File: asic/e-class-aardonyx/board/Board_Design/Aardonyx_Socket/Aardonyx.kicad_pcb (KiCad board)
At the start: 4 copper layers, 188.6 x 147.6 mm, 327 parts, among them J1 USB_B_6PIN, J10 Conn_1x6, J11 Conn_1x6, J12 Conn_1x3_M, J13 Conn_1x8_F, J14 Conn_1x6_F, J15 Conn_1x10_F, J16 Conn_1x8_F, J17 USB_OTG, J18 Conn_1x3_M, J19 Conn_1x3_M, J2 Conn_1x8, J3 Conn_1x3_M, J4 Conn_1x4, J5 PJ-202H PWRJACK, J6 Conn_1x3_M, J7 Conn_1x4, J8 Conn_1x3_M, J9 Conn_1x8, Q1 FDN339AN, SW1 SW_SPST, SW2 FSM2JSMAATR, SW3 SW_DIP_x03, U1 FT2232H, U10 TPS7A7002DDAR, U11 ADM1186, U13 TPS7A7002DDAR, U14 74AUP1G09GW, U15 SKT32E, U16 93LC56BT-I_OT, U2 IS42S32160F-TSOP2, U3 CDCE913PW, U4 TPS54627DDAR, U5 CAT24M01WI-GT3, U6 IS25LP256x-xM, U7 ADC128S102CIMTX/NOPB, U8 LSF0108PWR, U9 LSF0108PWR, Y1 12MHz, Y2 27MHz

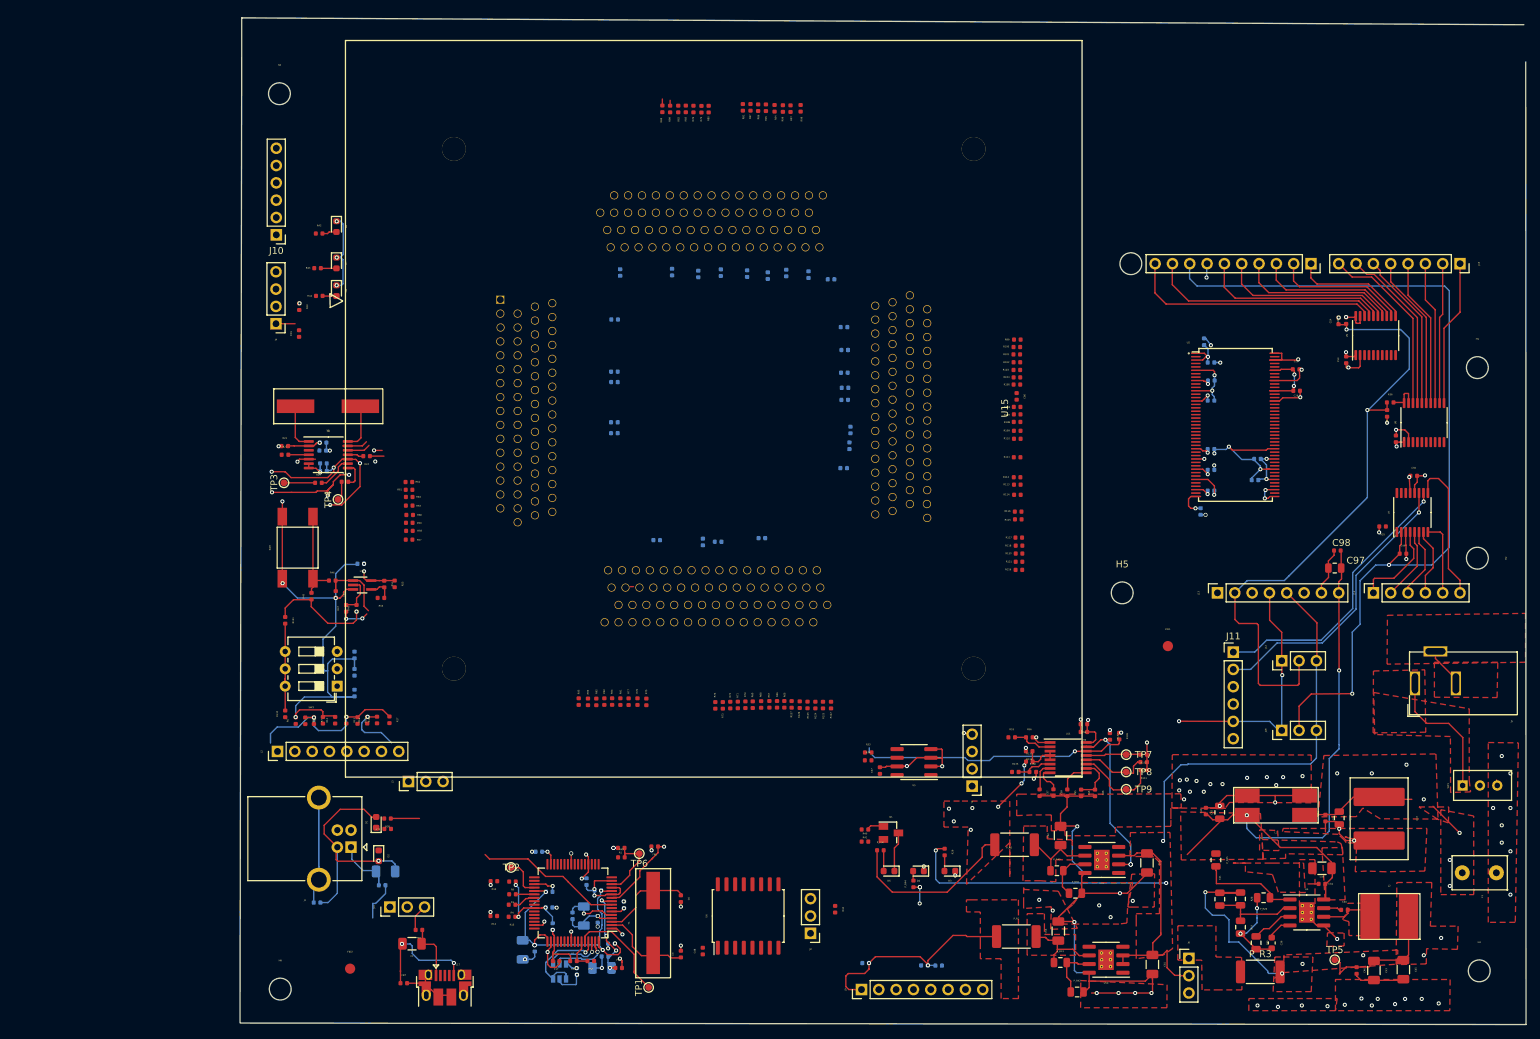
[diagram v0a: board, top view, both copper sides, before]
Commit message: updated socket com placement
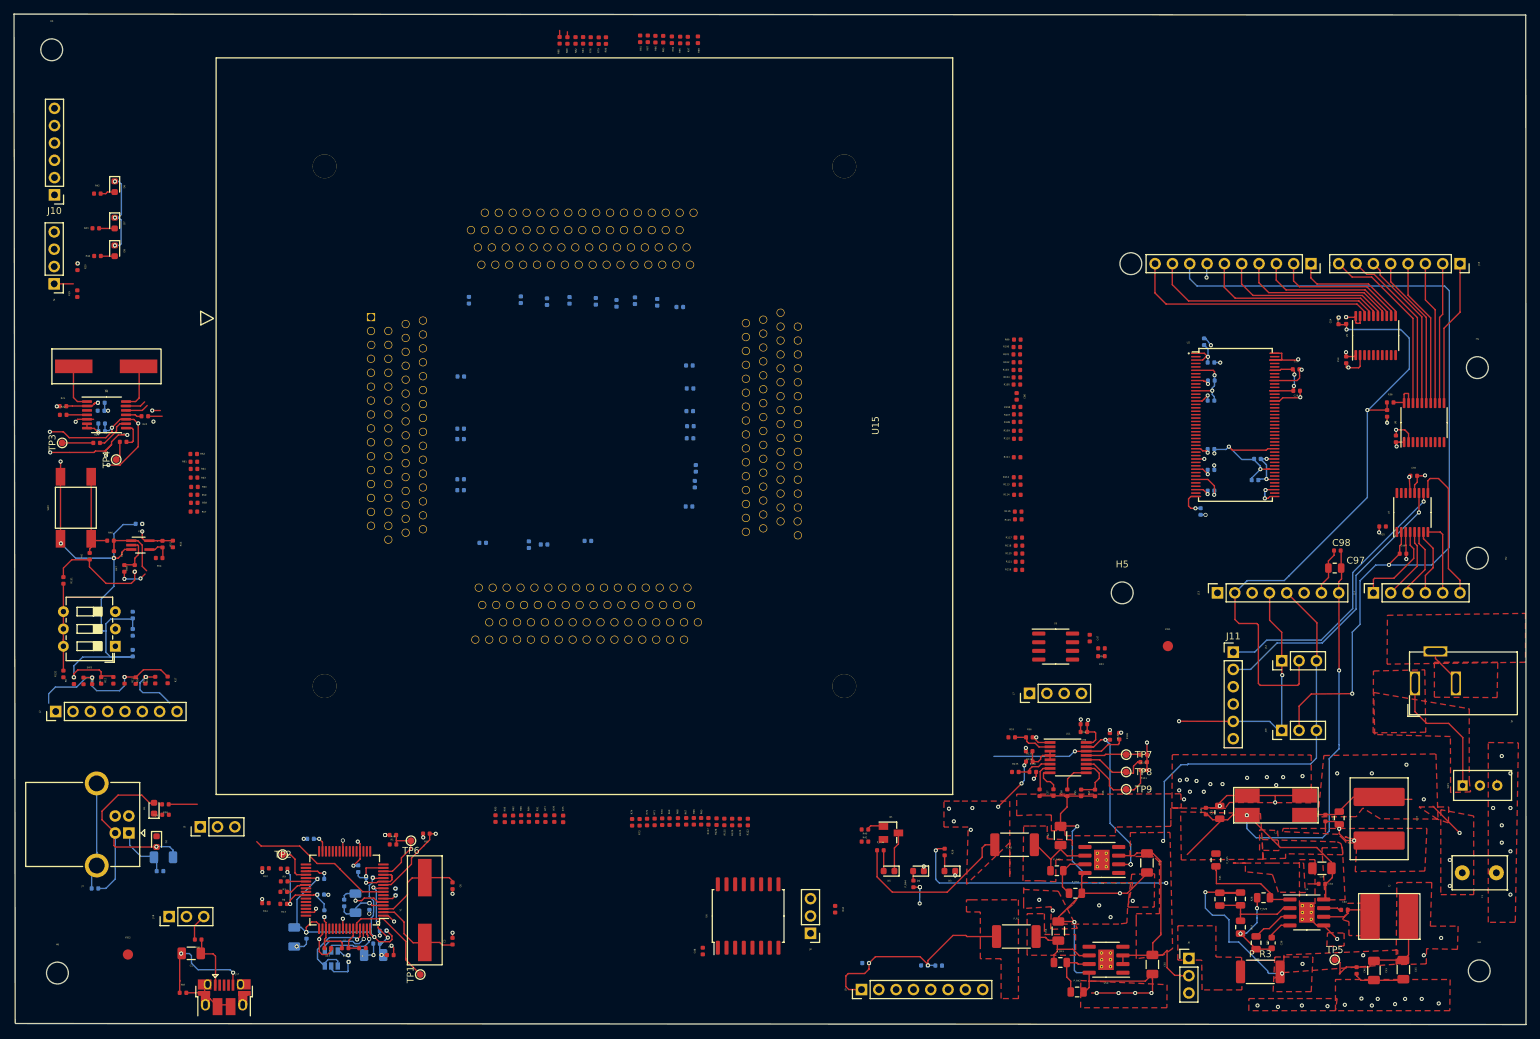
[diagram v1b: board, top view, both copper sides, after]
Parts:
- moved R34 37.9 mm to (218.2, 107.4), turned to 180 degrees
- moved R33 37.0 mm to (218.2, 108.5), turned to 180 degrees
- moved C47 36.4 mm to (216.4, 105.9), turned to 270 degrees
- moved H3 34.0 mm to (64.2, 19.6)
- moved C2 33.5 mm to (99.8, 149.7)
- moved C8 33.5 mm to (111.9, 150.7)
- moved R13 33.5 mm to (98.3, 144.9)
- moved R14 33.5 mm to (95.6, 144.8)
- moved C10 33.5 mm to (107.1, 144.7)
- moved C12 33.5 mm to (103.7, 141.2)
- moved C13 33.5 mm to (112.8, 148.8)
- moved C16 33.5 mm to (103.7, 143.5)
- moved C3 33.5 mm to (123.0, 150.3)
- moved C4 33.5 mm to (101.6, 149.5)
- moved C5 33.5 mm to (111.5, 152.4)
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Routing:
- net /power_2/RESET_ASIC: track 44.0 -> 24.4 mm
- net GND: track 506.5 -> 489.5 mm, vias 118 -> 115
- net VBUS_USB1: track 5.79 -> 0.00 mm
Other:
- board size 188.6 x 147.6 mm -> 221.7 x 148.2 mm

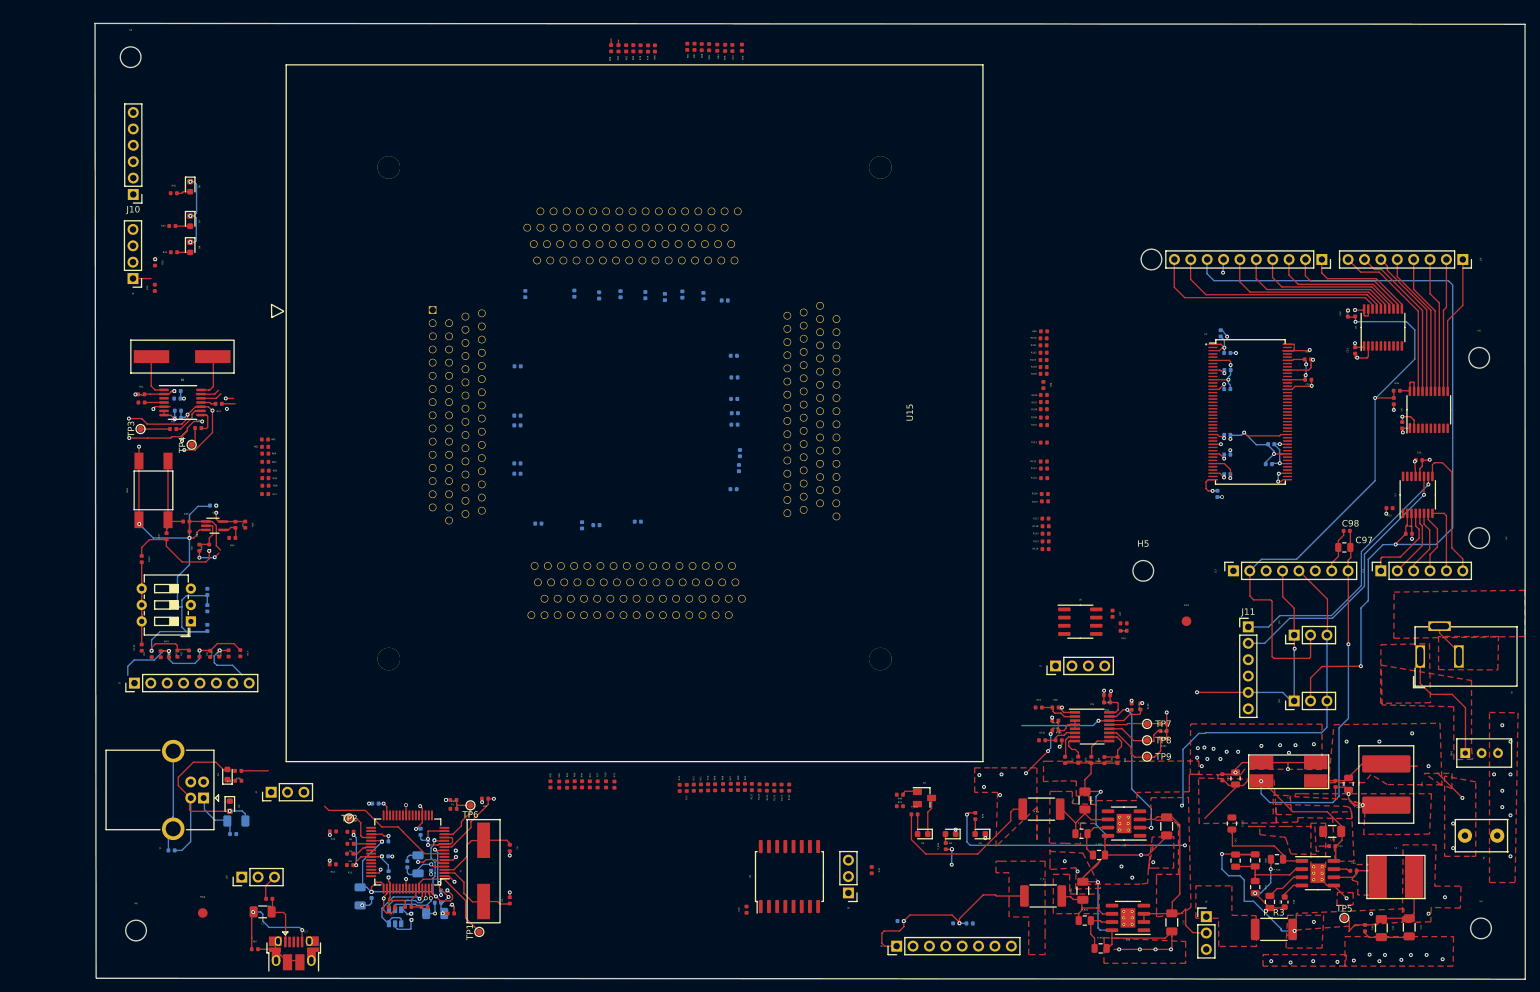
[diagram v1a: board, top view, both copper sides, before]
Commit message: update socket compo placement
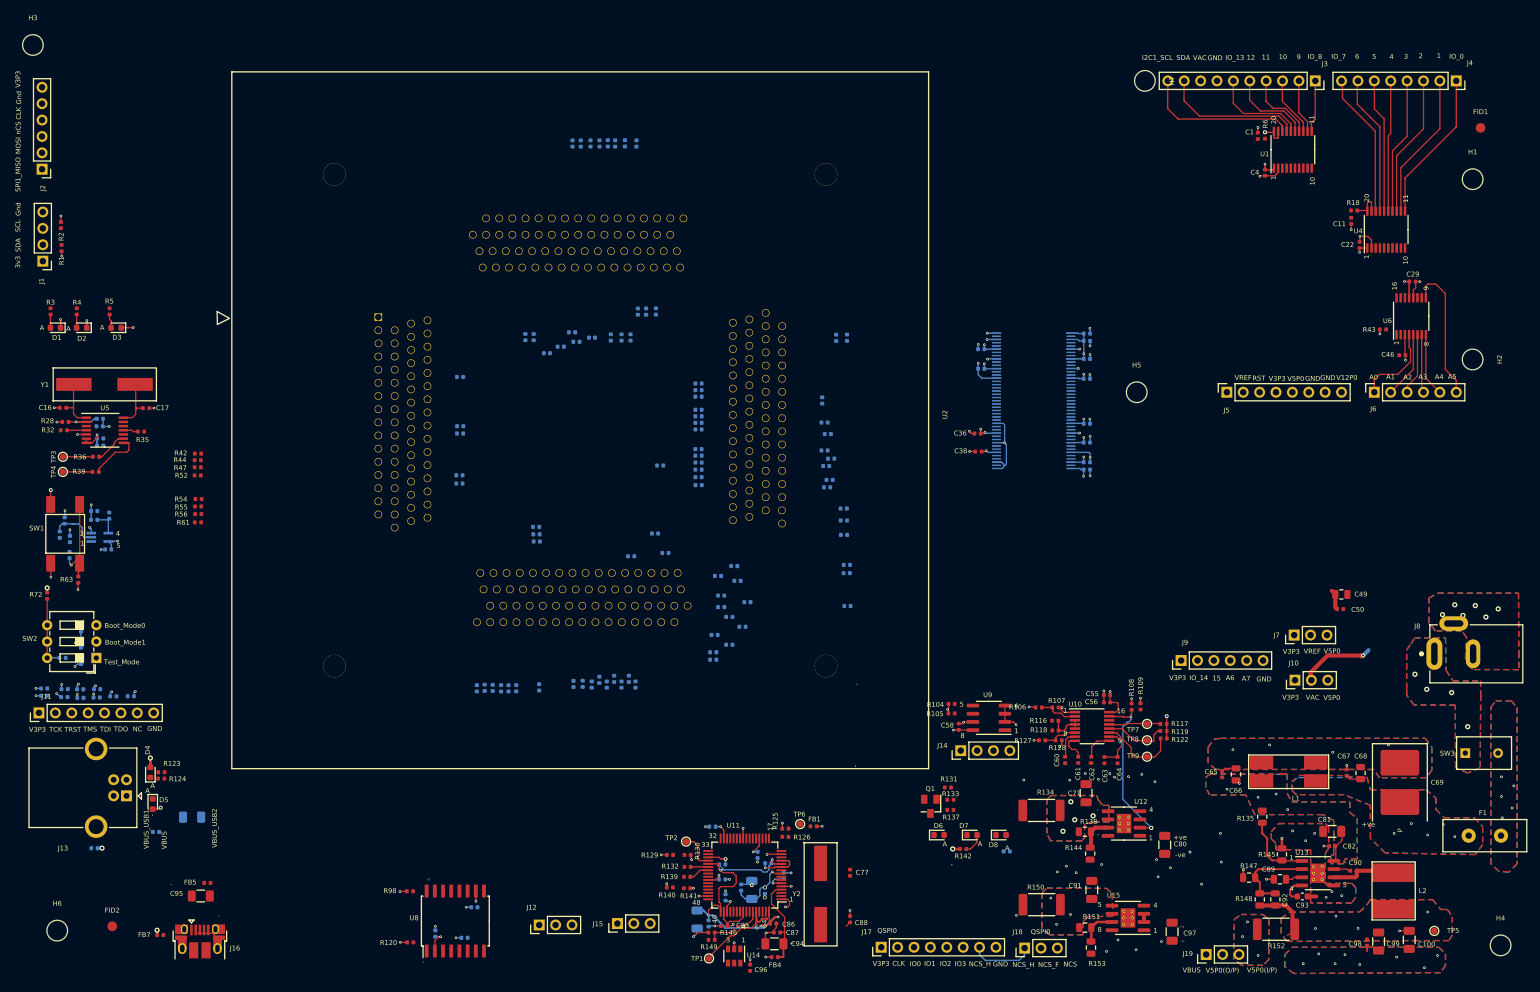
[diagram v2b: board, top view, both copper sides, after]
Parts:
- removed the C1 at (84.7, 152.1)
- removed the C10 at (107.1, 144.7)
- removed the C11 at (110.9, 141.0)
- removed the C12 at (103.7, 141.2)
- removed the C13 at (112.8, 148.8)
- removed the C15 at (102.2, 135.3)
- removed the C19 at (234.2, 65.5)
- removed the C2 at (99.8, 149.7)
- removed the C32 at (71.6, 75.6)
- removed the C36 at (243.1, 150.6)
- removed the C4 at (101.6, 149.5)
- removed the C47 at (216.4, 105.9)
- removed the C48 at (159.7, 151.8)
- removed the C5 at (111.5, 152.4)
- removed the C7 at (104.2, 146.3)
- removed the C71 at (124.2, 84.2)
- removed the C8 at (111.9, 150.7)
- removed the C9 at (108.8, 144.8)
- removed the D6 at (73.5, 39.7)
- removed the D7 at (73.5, 45.0)
- removed the D8 at (73.5, 49.1)
- removed the FB3 at (110.8, 145.2)
- removed the J10 at (64.7, 40.9)
- removed the J3 at (86.0, 133.6)
- removed the J4 at (64.6, 54.0)
- removed the J7 at (207.6, 114.0)
- removed the J8 at (175.5, 149.2)
- removed the R1 at (114.3, 134.8)
- removed the R10 at (95.6, 139.7)
- removed the R115 at (206.0, 88.5)
- removed the R116 at (205.9, 87.4)
- removed the R119 at (206.1, 95.9)
- removed the R14 at (95.6, 144.8)
- removed the R142 at (183.6, 153.5)
- removed the R20 at (68.0, 51.5)
- removed the R21 at (65.9, 71.9)
- removed the R30 at (194.3, 153.9)
- removed the R31 at (192.2, 153.9)
- removed the R32 at (179.1, 145.7)
- removed the R33 at (218.2, 108.5)
- removed the R34 at (218.2, 107.4)
- removed the R43 at (70.7, 45.8)
- removed the R44 at (71.0, 49.9)
- removed the R49 at (114.3, 136.2)
- removed the R50 at (109.8, 151.4)
- removed the R52 at (107.3, 151.4)
- removed the R62 at (85.1, 78.9)
- removed the R72 at (151.5, 132.9)
- removed the R8 at (71.5, 112.1)
- removed the R80 at (145.5, 18.3)
- removed the R83 at (142.2, 18.3)
- removed the R9 at (98.3, 139.7)
- removed the U1 at (107.2, 142.8)
- removed the U15 at (142.4, 74.8)
- removed the U5 at (211.5, 107.1)
- removed the U6 at (166.4, 146.6)
- removed the Y1 at (119.0, 145.8)
- added C28: 0.1UF,0402, Capacitor_SMD:C_0402_1005Metric, B.Cu at (59.5, 79.9)
- added C42: 0.1UF,0402, Capacitor_SMD:C_0402_1005Metric, B.Cu at (115.2, 85.7)
- added C57: 0.1UF,0402, Capacitor_SMD:C_0402_1005Metric, B.Cu at (111.5, 155.5)
- added C58: 0.1UF,0402, Capacitor_SMD:C_0402_1005Metric, F.Cu at (192.6, 123.4)
- added C59: 0.1UF,0402, Capacitor_SMD:C_0402_1005Metric, B.Cu at (154.4, 138.9)
- added C70: 0.1UF,0402, Capacitor_SMD:C_0402_1005Metric, B.Cu at (161.4, 143.3)
- added C72: 0.1UF,0402, Capacitor_SMD:C_0402_1005Metric, B.Cu at (156.0, 144.8)
- added C73: 0.1UF,0402, Capacitor_SMD:C_0402_1005Metric, B.Cu at (163.1, 144.6)
- added C75: 0.1UF,0402, Capacitor_SMD:C_0402_1005Metric, B.Cu at (156.5, 149.9)
- added C76: 0.1UF,0402, Capacitor_SMD:C_0402_1005Metric, B.Cu at (155.9, 147.1)
- added C78: 0.1UF,0402, Capacitor_SMD:C_0402_1005Metric, B.Cu at (158.9, 148.3)
- added C79: 4.7UF,1206, Capacitor_SMD:C_1206_3216Metric, B.Cu at (160.5, 148.7)
- added C83: 4.7UF,1206, Capacitor_SMD:C_1206_3216Metric, B.Cu at (152.1, 153.3)
- added C84: 0.1UF,0402, Capacitor_SMD:C_0402_1005Metric, B.Cu at (153.8, 153.9)
- added C85: 0.1UF,0402, Capacitor_SMD:C_0402_1005Metric, F.Cu at (156.2, 154.3)
- added C86: 0.1UF,0402, Capacitor_SMD:C_0402_1005Metric, F.Cu at (163.9, 153.9)
- added C87: 0.1UF,0402, Capacitor_SMD:C_0402_1005Metric, F.Cu at (164.4, 155.3)
- added C93: 7500PF,0603, Capacitor_SMD:C_0603_1608Metric, F.Cu at (245.9, 149.7)
- added C94: 4.7UF,1206, Capacitor_SMD:C_1206_3216Metric, F.Cu at (164.0, 157.1)
- added C95: 4.7UF,1206, Capacitor_SMD:C_1206_3216Metric, F.Cu at (75.1, 149.7)
- added D1: LED,1206, LED_SMD:LED_0603_1608Metric, F.Cu at (52.6, 61.6)
- added D2: LED,1206, LED_SMD:LED_0603_1608Metric, F.Cu at (56.7, 61.6)
- added D3: LED,1206, LED_SMD:LED_0603_1608Metric, F.Cu at (62.0, 61.6)
- added FB4: 600E,FB,0402, Inductor_SMD:L_0402_1005Metric, F.Cu at (164.1, 159.1)
- added J1: Conn_1x4, Connector_PinHeader_2.54mm:PinHeader_1x04_P2.54mm_Vertical, F.Cu at (50.6, 51.3)
- added J12: Conn_1x3_M, Connector_PinHeader_2.54mm:PinHeader_1x03_P2.54mm_Vertical, F.Cu at (127.6, 154.2)
- added J14: Conn_1x4, Connector_PinHeader_2.54mm:PinHeader_1x04_P2.54mm_Vertical, F.Cu at (192.9, 127.1)
- added J15: Conn_1x3_M, Connector_PinHeader_2.54mm:PinHeader_1x03_P2.54mm_Vertical, F.Cu at (139.7, 153.9)
- added J2: Conn_1x6, Connector_PinHeader_2.54mm:PinHeader_1x06_P2.54mm_Vertical, F.Cu at (50.5, 37.0)
- added R101: 1KE,0402, Resistor_SMD:R_0402_1005Metric, B.Cu at (56.4, 117.6)
- added R103: 10KE,0402, Resistor_SMD:R_0402_1005Metric, B.Cu at (117.5, 151.4)
- added R104: 10KE,0402, Resistor_SMD:R_0402_1005Metric, F.Cu at (191.5, 119.9)
- added R105: 10KE,0402, Resistor_SMD:R_0402_1005Metric, F.Cu at (191.5, 121.4)
- added R111: 1KE,0402, Resistor_SMD:R_0402_1005Metric, B.Cu at (54.0, 118.8)
- added R120: 10KE,0402, Resistor_SMD:R_0402_1005Metric, F.Cu at (107.6, 156.8)
- added R121: 10KE,0402, Resistor_SMD:R_0402_1005Metric, B.Cu at (116.0, 156.1)
- added R125: 1KE,0402, Resistor_SMD:R_0402_1005Metric, F.Cu at (165.7, 139.2)
- added R126: 0E, 0402, Resistor_SMD:R_0402_1005Metric, F.Cu at (165.7, 140.5)
- added R129: 1KE,0402, Resistor_SMD:R_0402_1005Metric, F.Cu at (147.8, 143.3)
- added R130: 1KE,0402, Resistor_SMD:R_0402_1005Metric, F.Cu at (150.6, 143.3)
- added R132: 0E, 0402, Resistor_SMD:R_0402_1005Metric, F.Cu at (150.6, 145.2)
- added R136: 12KE,0402, Resistor_SMD:R_0402_1005Metric, B.Cu at (165.5, 146.6)
- added R139: 0E, 0402, Resistor_SMD:R_0402_1005Metric, F.Cu at (150.5, 146.7)
- added R140: 1KE,0402, Resistor_SMD:R_0402_1005Metric, F.Cu at (147.8, 148.3)
- added R141: 1KE,0402, Resistor_SMD:R_0402_1005Metric, F.Cu at (150.5, 148.5)
- added R146: 10KE,0402, Resistor_SMD:R_0402_1005Metric, F.Cu at (154.3, 155.3)
- added R149: 4.7KE,0402, Resistor_SMD:R_0402_1005Metric, F.Cu at (154.3, 156.5)
- added R28: 4.7KE,0402, Resistor_SMD:R_0402_1005Metric, F.Cu at (54.1, 76.2)
- added R5: 220E,0402, Resistor_SMD:R_0402_1005Metric, F.Cu at (61.0, 59.0)
- added R58: 22E,0402, Resistor_SMD:R_0402_1005Metric, B.Cu at (172.8, 81.9)
- added R59: 22E,0402, Resistor_SMD:R_0402_1005Metric, B.Cu at (171.8, 80.6)
- added R77: 22E,0402, Resistor_SMD:R_0402_1005Metric, B.Cu at (157.0, 110.7)
- added R89: 22E,0402, Resistor_SMD:R_0402_1005Metric, B.Cu at (138.0, 116.9)
- added R98: 10KE,0402, Resistor_SMD:R_0402_1005Metric, F.Cu at (107.5, 148.9)
- added U10: ADM1186, Package_SO:QSOP-16_3.9x4.9mm_P0.635mm, F.Cu at (213.3, 123.4)
- added U3: IS42S32160F-TSOP2, Aardonyx:TSSOP-II-86_10.16x22.2mm_P0.5mm, B.Cu at (204.2, 72.9)
- added U8: IS25LP256x-xM, Package_SO:SOIC-16W_7.5x10.3mm_P1.27mm, F.Cu at (114.6, 153.5)
- added U9: CAT24M01WI-GT3, Package_SO:SOIC-8_3.9x4.9mm_P1.27mm, F.Cu at (197.3, 122.0)
- added Y2: 12MHz, Aardonyx:Crystal_SMD_ROHS_CSM_7XDN_HandSoldering, F.Cu at (171.2, 149.4)
- C15: renamed from C28; moved to B.Cu
- C16: value 0.1UF,0402 -> 18PF,0402; moved to F.Cu
- C17: value 0.1UF,0402 -> 18PF,0402
- C25: renamed from C86; moved to B.Cu
- C36: renamed from C26; moved to F.Cu
- C38: renamed from C25; moved to F.Cu
- C40: renamed from C29; moved to B.Cu
- C44: renamed from C60; moved to B.Cu
- C69: renamed from C37; footprint Aardonyx:CP_EIA-7260-38_VISHAY_Pad2.68x7.50mm_HandSolder -> Aardonyx:CP_EIA-2924_tcn4227_Pad6.1x7.3mm
- C96: renamed from C92; moved to F.Cu
- F1: footprint Aardonyx:vishay_ptccl_d1mm_w5mm -> Aardonyx:vishay_ptccl_d12.5mm_w4mm
- FB2, R51, R75, R76: moved to B.Cu
- J8: renamed from J5; footprint Aardonyx:Pwr_Jack_DC_PJ-202AH_Horizontal -> Aardonyx:CUI_PJ-202AH
- R10: renamed from R82; moved to B.Cu
- R100: renamed from R7; moved to B.Cu
- R102: renamed from R16; moved to B.Cu
- R11, R13: value 1KE,0402 -> 22E,0402; moved to B.Cu
- R110: renamed from R6; moved to B.Cu
- R112: renamed from R12; moved to B.Cu
- R113: renamed from R15; moved to B.Cu
- R114: renamed from R18; moved to B.Cu
- R115: renamed from R17; moved to B.Cu
- R12: renamed from R78; moved to B.Cu
- R14: renamed from R87; moved to B.Cu
- R143: renamed from R29; moved to B.Cu
- R15: renamed from R86; moved to B.Cu
- R16: renamed from R85; moved to B.Cu
- R17: renamed from R84; moved to B.Cu
- R19: renamed from R81; moved to B.Cu
- R2: value 12KE,0402 -> 4.7KE,0402; moved to F.Cu
- R20: renamed from R99; moved to B.Cu
- R21: renamed from R79; moved to B.Cu
- R22: renamed from R100; moved to B.Cu
- R23: renamed from R88; moved to B.Cu
- R24: renamed from R89; moved to B.Cu
- R25: renamed from R101; moved to B.Cu
- R26: renamed from R102; moved to B.Cu
- R27: renamed from R103; moved to B.Cu
- R3, R4: value 0E, 0402 -> 220E,0402
- R30: renamed from R104; moved to B.Cu
- R31: renamed from R105; moved to B.Cu
- R33: renamed from R106; moved to B.Cu
- R34: renamed from R107; moved to B.Cu
- R37: renamed from R108; moved to B.Cu
- R38: renamed from R109; moved to B.Cu
- R40: renamed from R110; moved to B.Cu
- R41: renamed from R111; moved to B.Cu
- R42: value 220E,0402 -> 22E,0402
- R45: renamed from R55; moved to B.Cu
- R46: renamed from R54; moved to B.Cu
- R48: renamed from R112; moved to B.Cu
- R49: renamed from R113; moved to B.Cu
- R50: renamed from R48; moved to B.Cu
- R53: renamed from R47; moved to B.Cu
- R57: renamed from R114; moved to B.Cu
- R60: renamed from R46; moved to B.Cu
- R62: renamed from R117; moved to B.Cu
- R64: renamed from R124; moved to B.Cu
- R65: renamed from R122; moved to B.Cu
- R66: renamed from R120; moved to B.Cu
- R67: renamed from R118; moved to B.Cu
- R68: renamed from R125; moved to B.Cu
- R69: renamed from R123; moved to B.Cu
- R7: renamed from R96; moved to B.Cu
- R70: renamed from R121; moved to B.Cu
- R71: renamed from R126; moved to B.Cu
- R73: renamed from R77; moved to B.Cu
- R74: renamed from R127; moved to B.Cu
- R78: renamed from R65; moved to B.Cu
- R79: renamed from R66; moved to B.Cu
- R8: renamed from R97; moved to B.Cu
- R81: renamed from R95; moved to B.Cu
- R82: renamed from R93; moved to B.Cu
- R83: renamed from R92; moved to B.Cu
- R84: renamed from R90; moved to B.Cu
- R85: renamed from R94; moved to B.Cu
- R86: renamed from R91; moved to B.Cu
- R87: renamed from R74; moved to B.Cu
- R88: renamed from R73; moved to B.Cu
- R9: renamed from R98; moved to B.Cu
- R90: renamed from R71; moved to B.Cu
- R91: renamed from R70; moved to B.Cu
- R92: renamed from R69; moved to B.Cu
- R93: renamed from R68; moved to B.Cu
- R94: renamed from R67; moved to B.Cu
- R96: renamed from R132; moved to B.Cu
- R99: renamed from R5; moved to B.Cu
- U11: value ADM1186 -> FT2232H; footprint Package_SO:QSOP-16_3.9x4.9mm_P0.635mm -> Package_QFP:LQFP-64_10x10mm_P0.5mm
- U14: renamed from U16; moved to F.Cu
- U2: value IS42S32160F-TSOP2 -> SKT32E; footprint Aardonyx:TSSOP-II-86_10.16x22.2mm_P0.5mm -> Aardonyx:SKT32E_IITM_TH_SOCKET
- U7: renamed from U14; moved to B.Cu
- moved C14 128.3 mm to (212.5, 63.6), turned to 0 degrees
- moved J18 121.8 mm to (202.8, 157.7)
- moved R13 118.8 mm to (138.2, 33.0), turned to 90 degrees
- moved R2 115.1 mm to (53.4, 45.7), turned to 270 degrees
- moved U2 103.9 mm to (133.9, 75.9), turned to 270 degrees
- moved R11 103.0 mm to (140.9, 33.0), turned to 90 degrees
- moved R3 94.7 mm to (51.8, 59.0), turned to 270 degrees
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- renumbered C54 to C1, C88 to C10, C45 to C100, C52 to C11, C18 to C12, C64 to C13, C20 to C18, C65 to C19, C82 to C2, C89 to C20, C27 to C21, C51 to C22, C30 to C23, C87 to C24, C21 to C26, C31 to C27, C50 to C29, C79 to C3, C84 to C30, C63 to C31, C68 to C32, C83 to C33, C81 to C34, C22 to C35, C78 to C37, C80 to C39, C53 to C4, C66 to C41, C23 to C43, C24 to C45, C49 to C46, C61 to C47, C75 to C48, C97 to C49, C76 to C5, C98 to C50, C74 to C51, C69 to C52, C77 to C53, C72 to C54, C94 to C55, C93 to C56, C73 to C6, C57 to C60, C58 to C61, C85 to C62, C95 to C63, C96 to C64, C44 to C65, C42 to C66, C39 to C67, C38 to C68, C90 to C7, C62 to C71, C91 to C74, C6 to C77, C70 to C8, C59 to C80, C33 to C81, C34 to C82, C3 to C88, C35 to C89, C67 to C9, C40 to C90, C56 to C91, C41 to C92, C55 to C97, C46 to C98, C43 to C99, D1 to D4, D2 to D5, D5 to D6, D4 to D7, D3 to D8, FB6 to FB3, FB4 to FB6, J19 to J10, J2 to J11, J1 to J13, J17 to J16, J9 to J17, J6 to J19, J15 to J3, J16 to J4, J13 to J5, J14 to J6, J12 to J7, J11 to J9, R19 to R1, R53 to R106, R56 to R107, R137 to R108, R138 to R109, R134 to R116, R139 to R117, R133 to R118, R140 to R119, R141 to R122, R38 to R123, R39 to R124, R135 to R127, R136 to R128, R40 to R131, R41 to R133, P_R2 to R134, P_R25 to R135, P_R56 to R137, P_R49 to R138, P_R44 to R142, P_R50 to R144, P_R26 to R145, R27 to R147, R28 to R148, P_R1 to R150, P_R41 to R151, P_R3 to R152, P_R42 to R153, R36 to R18, R23 to R29, R22 to R32, R24 to R35, R25 to R36, R26 to R39, R35 to R43, R61 to R44, R64 to R47, R63 to R52, R60 to R54, R59 to R55, R58 to R56, R37 to R6, R57 to R61, R45 to R63, R131 to R72, R128 to R80, R129 to R95, R130 to R97, SW2 to SW1, SW3 to SW2, SW1 to SW3, U9 to U1, U13 to U12, U4 to U13, U10 to U15, U8 to U4, U3 to U5, U7 to U6, Y2 to Y1
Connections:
- net /ftdi/USB_DM renamed /ftdi/USB_D-
- net /ftdi/USB_DP renamed /ftdi/USB_D+
- C16 pad 1: V3P3 -> Net-(C16-Pad1)
- C17 pad 1: V3P3 -> Net-(C17-Pad1)
- C60 pad 1: Net-(C57-Pad1) -> Net-(C60-Pad1)
- C61 pad 1: Net-(C58-Pad1) -> Net-(C61-Pad1)
- C62 pad 1: Net-(C85-Pad1) -> Net-(C62-Pad1)
- C63 pad 1: Net-(C95-Pad1) -> Net-(C63-Pad1)
- C64 pad 1: Net-(C95-Pad1) -> Net-(C63-Pad1)
- C71 pad 1: Net-(C62-Pad1) -> Net-(C71-Pad1)
- C77 pad 1: Net-(C6-Pad1) -> Net-(C77-Pad1)
- C88 pad 1: Net-(C3-Pad1) -> Net-(C88-Pad1)
- C91 pad 1: Net-(C56-Pad1) -> Net-(C91-Pad1)
- FB1 pad 1: Net-(C1-Pad1) -> GNDA
- FB1 pad 2: VBUS_USB2 -> GND
- FB2 pad 1: Net-(C5-Pad1) -> Net-(C78-Pad1)
- FB5 pad 1: GNDA -> Net-(C95-Pad1)
- FB5 pad 2: GND -> VBUS_USB2
- J11 pad 2: /ftdi/TRST -> /ftdi/TCK
- J11 pad 3: /ftdi/TMS -> /ftdi/TRST
- J11 pad 4: /soc/TD0 -> /ftdi/TMS
- J11 pad 6: /ftdi/TCK -> /soc/TD0
- J16 pad 1: Net-(C1-Pad1) -> Net-(C95-Pad1)
- J18 pad 1: VBUS_USB1 -> /arduino_header/QSPI0_NCS_H
- J18 pad 2: VBUS -> /arduino_header/QSPI0_NCS_F
- J18 pad 3: VBUS_USB2 -> /arduino_header/QSPI0_NCS
- J19 pad 1: Net-(J6-Pad1) -> VBUS
- J19 pad 3: VBUS -> Net-(J19-Pad3)
- J9 pad 1: /arduino_header/A6 -> V3P3
- J9 pad 2: /arduino_header/A7 -> /arduino_header/IO_14
- J9 pad 3: /arduino_header/IO_14 -> /arduino_header/IO_15
- J9 pad 4: /arduino_header/IO_15 -> /arduino_header/A6
- J9 pad 5: V3P3 -> /arduino_header/A7
- R10 pad 1: Net-(R82-Pad1) -> Net-(R10-Pad1)
- R100 pad 2: /ftdi/TMS -> /ftdi/TRST
- R11 pad 1: V3P3 -> Net-(R11-Pad1)
- R11 pad 2: /soc/TD0 -> /sdram/SDRAM_BA1
- R110 pad 1: /ftdi/TRST -> /ftdi/TCK
- R112 pad 1: /soc/TD0 -> /ftdi/TMS
- R114 pad 1: /ftdi/TCK -> /soc/TD0
- R115 pad 2: /ftdi/TCK -> /soc/TD0
- R12 pad 1: Net-(R78-Pad1) -> Net-(R12-Pad1)
- R123 pad 1: Net-(R38-Pad1) -> /ftdi/D+
- R124 pad 1: Net-(R39-Pad1) (its old number) -> /ftdi/D-
- R13 pad 1: V3P3 -> Net-(R13-Pad1)
- R13 pad 2: /ftdi/UART0_TX -> /sdram/SDRAM_DQM2
- R134 pad 2: Net-(C62-Pad1) -> Net-(C71-Pad1)
- R138 pad 1: Net-(C62-Pad1) -> Net-(C71-Pad1)
- R14 pad 1: Net-(R87-Pad1) -> Net-(R14-Pad1)
- R15 pad 1: Net-(R86-Pad1) -> Net-(R15-Pad1)
- R150 pad 2: Net-(C56-Pad1) -> Net-(C91-Pad1)
- R151 pad 1: Net-(C56-Pad1) -> Net-(C91-Pad1)
- R152 pad 1: Net-(J6-Pad1) -> Net-(J19-Pad3)
- R16 pad 1: Net-(R85-Pad1) -> Net-(R16-Pad1)
- R17 pad 1: Net-(R84-Pad1) -> Net-(R17-Pad1)
- R19 pad 1: Net-(R81-Pad1) -> Net-(R19-Pad1)
- R2 pad 1: Net-(R2-Pad1) -> V3P3
- R2 pad 2: GND -> Net-(J1-Pad3)
- R20 pad 2: Net-(R99-Pad2) -> Net-(R20-Pad2)
- R21 pad 1: Net-(R79-Pad1) -> Net-(R21-Pad1)
- R22 pad 2: Net-(R100-Pad2) -> Net-(R22-Pad2)
- R23 pad 1: Net-(R88-Pad1) -> Net-(R23-Pad1)
- R24 pad 1: Net-(R89-Pad1) -> Net-(R24-Pad1)
- R25 pad 2: Net-(R101-Pad2) -> Net-(R25-Pad2)
- R26 pad 2: Net-(R102-Pad2) -> Net-(R26-Pad2)
- R27 pad 2: Net-(R103-Pad2) -> Net-(R27-Pad2)
- R3 pad 1: Net-(R3-Pad1) -> /arduino_header/IO_15
- R3 pad 2: /ftdi/UART0_RX -> Net-(D1-Pad2)
- R30 pad 2: Net-(R104-Pad2) -> Net-(R30-Pad2)
- R31 pad 2: Net-(R105-Pad2) -> Net-(R31-Pad2)
- R33 pad 2: Net-(R106-Pad2) -> Net-(R33-Pad2)
- R34 pad 2: Net-(R107-Pad2) -> Net-(R34-Pad2)
- R37 pad 2: Net-(R108-Pad2) -> Net-(R37-Pad2)
- R38 pad 2: Net-(R109-Pad2) -> Net-(R38-Pad2)
- R4 pad 1: Net-(R4-Pad1) -> /arduino_header/IO_14
- R4 pad 2: /ftdi/UART0_TX -> Net-(D2-Pad2)
- R40 pad 2: Net-(R110-Pad2) -> Net-(R40-Pad2)
- R41 pad 2: Net-(R111-Pad2) -> Net-(R41-Pad2)
- R42 pad 1: /arduino_header/IO_13 -> Net-(R42-Pad1)
- R42 pad 2: Net-(D6-Pad2) (its old number) -> /arduino_header/SPI1_CLK
- R44 pad 1: Net-(R61-Pad1) -> Net-(R44-Pad1)
- R47 pad 1: Net-(R64-Pad1) -> Net-(R47-Pad1)
- R48 pad 2: Net-(R112-Pad2) -> Net-(R48-Pad2)
- R49 pad 2: Net-(R113-Pad2) -> Net-(R49-Pad2)
- R52 pad 1: Net-(R63-Pad1) -> Net-(R52-Pad1)
- R54 pad 1: Net-(R60-Pad1) (its old number) -> Net-(R54-Pad1)
- R55 pad 1: Net-(R59-Pad1) -> Net-(R55-Pad1)
- R56 pad 1: Net-(R58-Pad1) -> Net-(R56-Pad1)
- R57 pad 2: Net-(R114-Pad2) -> Net-(R57-Pad2)
- R61 pad 1: Net-(R57-Pad1) -> Net-(R61-Pad1)
- R62 pad 2: Net-(R117-Pad2) -> Net-(R62-Pad2)
- R64 pad 2: Net-(R124-Pad2) -> Net-(R64-Pad2)
- R65 pad 2: Net-(R122-Pad2) -> Net-(R65-Pad2)
- R66 pad 2: Net-(R120-Pad2) -> Net-(R66-Pad2)
- R67 pad 2: Net-(R118-Pad2) -> Net-(R67-Pad2)
- R68 pad 2: Net-(R125-Pad2) -> Net-(R68-Pad2)
- R69 pad 2: Net-(R123-Pad2) -> Net-(R69-Pad2)
- R7 pad 2: Net-(R96-Pad2) -> Net-(R7-Pad2)
- R70 pad 2: Net-(R121-Pad2) -> Net-(R70-Pad2)
- R71 pad 2: Net-(R126-Pad2) -> Net-(R71-Pad2)
- R73 pad 1: Net-(R77-Pad1) -> Net-(R73-Pad1)
- R74 pad 2: Net-(R127-Pad2) -> Net-(R74-Pad2)
- R75 pad 1: Net-(R75-Pad1) -> /sdram/SDRAM_D23
- R75 pad 2: /sdram/SDRAM_A10 -> Net-(R75-Pad2)
- R78 pad 1: Net-(R65-Pad1) -> Net-(R78-Pad1)
- R79 pad 1: Net-(R66-Pad1) -> Net-(R79-Pad1)
- R8 pad 2: Net-(R97-Pad2) -> Net-(R8-Pad2)
- R81 pad 2: Net-(R95-Pad2) -> Net-(R81-Pad2)
- R82 pad 2: Net-(R93-Pad2) -> Net-(R82-Pad2)
- R83 pad 2: Net-(R92-Pad2) -> Net-(R83-Pad2)
- R84 pad 2: Net-(R90-Pad2) -> Net-(R84-Pad2)
- R85 pad 2: Net-(R94-Pad2) -> Net-(R85-Pad2)
- R86 pad 2: Net-(R91-Pad2) -> Net-(R86-Pad2)
- R87 pad 1: Net-(R74-Pad1) -> Net-(R87-Pad1)
- R88 pad 1: Net-(R73-Pad1) -> Net-(R88-Pad1)
- R9 pad 2: Net-(R98-Pad2) -> Net-(R9-Pad2)
- R90 pad 1: Net-(R71-Pad1) -> Net-(R90-Pad1)
- R91 pad 1: Net-(R70-Pad1) -> Net-(R91-Pad1)
- R92 pad 1: Net-(R69-Pad1) -> Net-(R92-Pad1)
- R93 pad 1: Net-(R68-Pad1) -> Net-(R93-Pad1)
- R94 pad 1: Net-(R67-Pad1) -> Net-(R94-Pad1)
- R99 pad 2: /ftdi/TRST -> /ftdi/TCK
- U11 pad 10: Net-(C95-Pad1) -> GNDA
- U11 pad 11: /power_2/PWR_GOOD -> GND
- U11 pad 12: /power_2/OUT4 -> VCORE_FTDI
- U11 pad 13: /power_2/OUT3 -> GND
- U11 pad 14: /power_2/RESET_ASIC -> /ftdi/FT_RESET
- U11 pad 15: /power_2/V18_EN -> GND
- U11 pad 16: V3P3 -> /ftdi/TCK
- U11 pad 2: /power_2/V3P3_MON -> Net-(C88-Pad1)
- U11 pad 3: /power_2/V1P8_MON -> Net-(C77-Pad1)
- U11 pad 4: /power_2/V1P8_MON -> Net-(C87-Pad1)
- U11 pad 5: /power_2/V1P8_MON -> GND
- U11 pad 6: /power_2/UP_DOWN# -> Net-(R136-Pad1)
- U11 pad 7: Net-(C57-Pad1) -> /ftdi/D-
- U11 pad 8: Net-(C58-Pad1) -> /ftdi/D+
- U11 pad 9: Net-(C85-Pad1) -> Net-(C78-Pad1)
- U12 pad 1: Net-(U13-Pad1) -> GND
- U12 pad 4: Net-(U13-Pad4) -> V5P0
- U12 pad 5: Net-(U13-Pad5) -> Net-(C71-Pad1)
- U12 pad 6: Net-(C62-Pad1) -> Net-(C71-Pad1)
- U12 pad 9: (no net) -> GND
- U14 pad 1: Net-(U1-Pad61) -> Net-(U11-Pad61)
- U14 pad 3: Net-(U1-Pad61) -> Net-(U11-Pad61)
- U14 pad 4: Net-(U1-Pad62) -> Net-(U11-Pad62)
- U14 pad 5: Net-(U1-Pad63) -> Net-(U11-Pad63)
- U15 pad 1: Net-(U10-Pad1) -> GND
- U15 pad 4: Net-(U10-Pad4) -> V5P0
- U15 pad 5: Net-(U10-Pad5) -> Net-(C91-Pad1)
- U15 pad 6: Net-(C56-Pad1) -> Net-(C91-Pad1)
- U15 pad 9: (no net) -> GND
- U2 pad 1: V3P3 -> Net-(U2-Pad1)
- U2 pad 10: /sdram/SDRAM_D5 -> /arduino_header/IO_13
- U2 pad 11: /sdram/SDRAM_D6 -> /arduino_header/IO_14
- U2 pad 12: GND -> Net-(U2-Pad12)
- U2 pad 13: /sdram/SDRAM_D7 -> Net-(U2-Pad13)
- U2 pad 14: Net-(U2-Pad14) -> /arduino_header/IO_15
- U2 pad 16: /sdram/SDRAM_DQM0 -> GND
- U2 pad 17: /sdram/SDRAM_WE -> Net-(U2-Pad17)
- U2 pad 18: /sdram/SDRAM_CAS -> /ftdi/UART0_TX
- U2 pad 19: /sdram/SDRAM_RAS -> Net-(U2-Pad19)
- U2 pad 2: /sdram/SDRAM_D0 -> /arduino_header/IO_10
- U2 pad 20: /sdram/SDRAM_CS -> /ftdi/UART0_RX
- U2 pad 21: /sdram/SDRAM_A11 -> Net-(U2-Pad21)
- U2 pad 22: /sdram/SDRAM_BA0 -> Net-(U2-Pad22)
- U2 pad 23: /sdram/SDRAM_BA1 -> /sdram/CLK
- U2 pad 24: /sdram/SDRAM_A10 -> /RESET
- U2 pad 25: /sdram/SDRAM_A0 -> /soc/BOOT_MODE0
- U2 pad 26: /sdram/SDRAM_A1 -> /soc/BOOT_MODE1
- U2 pad 27: /sdram/SDRAM_A2 -> /soc/TEST_MODE
- U2 pad 28: /sdram/SDRAM_DQM2 -> /ftdi/TCK
- U2 pad 29: V3P3 -> /ftdi/TRST
- U2 pad 3: V3P3 -> Net-(U2-Pad3)
- U2 pad 30: Net-(U2-Pad30) -> V1P8
- U2 pad 31: /sdram/SDRAM_D16 -> GND
- U2 pad 32: GND -> V3P3
- U2 pad 33: /sdram/SDRAM_D17 -> GND
- U2 pad 34: /sdram/SDRAM_D18 -> /ftdi/TMS
- U2 pad 35: V3P3 -> /ftdi/TDI
- U2 pad 36: /sdram/SDRAM_D19 -> /soc/TD0
- U2 pad 37: /sdram/SDRAM_D20 -> /arduino_header/I2C0_SDA
- U2 pad 38: GND -> /arduino_header/I2C0_SCL
- U2 pad 39: /sdram/SDRAM_D21 -> Net-(U2-Pad39)
- U2 pad 4: /sdram/SDRAM_D1 -> Net-(U2-Pad4)
- U2 pad 40: /sdram/SDRAM_D22 -> Net-(R42-Pad1)
- U2 pad 41: V3P3 -> Net-(R44-Pad1)
- U2 pad 42: /sdram/SDRAM_D23 -> Net-(R47-Pad1)
- U2 pad 43: V3P3 -> Net-(U2-Pad43)
- U2 pad 44: GND -> Net-(R52-Pad1)
- U2 pad 45: /sdram/SDRAM_D24 -> V1P8
- U2 pad 47: /sdram/SDRAM_D25 -> V3P3
- U2 pad 48: /sdram/SDRAM_D26 -> GND
- U2 pad 49: V3P3 -> Net-(R54-Pad1)
- U2 pad 5: /sdram/SDRAM_D2 -> /arduino_header/IO_11
- U2 pad 50: /sdram/SDRAM_D27 -> Net-(R55-Pad1)
- U2 pad 51: /sdram/SDRAM_D28 -> Net-(R56-Pad1)
- U2 pad 52: GND -> Net-(U2-Pad52)
- U2 pad 53: /sdram/SDRAM_D29 -> Net-(R61-Pad1)
- U2 pad 54: /sdram/SDRAM_D30 -> /arduino_header/I2C1_SCL
- U2 pad 55: V3P3 -> Net-(U2-Pad55)
- U2 pad 56: /sdram/SDRAM_D31 -> Net-(U2-Pad56)
- U2 pad 58: GND -> /arduino_header/I2C1_SDA
- U2 pad 59: /sdram/SDRAM_DQM3 -> Net-(U2-Pad59)
- U2 pad 6: GND -> Net-(U2-Pad6)
- U2 pad 60: /sdram/SDRAM_A3 -> Net-(U2-Pad60)
- U2 pad 61: /sdram/SDRAM_A4 -> Net-(U2-Pad61)
- U2 pad 62: /sdram/SDRAM_A5 -> Net-(U2-Pad62)
- U2 pad 63: /sdram/SDRAM_A6 -> Net-(U2-Pad63)
- U2 pad 64: /sdram/SDRAM_A7 -> Net-(U2-Pad64)
- U2 pad 65: /sdram/SDRAM_A8 -> Net-(U2-Pad65)
- U2 pad 66: /sdram/SDRAM_A9 -> Net-(R83-Pad2)
- U2 pad 67: /sdram/SDRAM_CKE -> Net-(U2-Pad67)
- U2 pad 68: /sdram/SDRAM_CLK -> Net-(U2-Pad68)
- U2 pad 69: /sdram/SDRAM_A12 -> Net-(U2-Pad69)
- U2 pad 7: /sdram/SDRAM_D3 -> Net-(U2-Pad7)
- U2 pad 70: Net-(U2-Pad70) -> Net-(R82-Pad2)
- U2 pad 71: /sdram/SDRAM_DQM1 -> Net-(R81-Pad2)
- U2 pad 72: GND -> Net-(R84-Pad2)
- U2 pad 73: Net-(U2-Pad73) -> Net-(R85-Pad2)
- U2 pad 74: /sdram/SDRAM_D8 -> Net-(R86-Pad2)
- U2 pad 75: V3P3 -> Net-(R73-Pad1)
- U2 pad 76: /sdram/SDRAM_D9 -> Net-(R76-Pad1)
- U2 pad 77: /sdram/SDRAM_D10 -> Net-(R77-Pad1)
- U2 pad 78: GND -> Net-(U2-Pad78)
- U2 pad 79: /sdram/SDRAM_D11 -> V3P3
- U2 pad 8: /sdram/SDRAM_D4 -> /arduino_header/IO_12
- U2 pad 80: /sdram/SDRAM_D12 -> GND
- U2 pad 81: V3P3 -> Net-(U2-Pad81)
- U2 pad 82: /sdram/SDRAM_D13 -> Net-(U2-Pad82)
- U2 pad 83: /sdram/SDRAM_D14 -> Net-(U2-Pad83)
- U2 pad 84: GND -> Net-(U2-Pad84)
- U2 pad 85: /sdram/SDRAM_D15 -> Net-(U2-Pad85)
- U2 pad 86: GND -> Net-(U2-Pad86)
- U2 pad 9: V3P3 -> Net-(U2-Pad9)
- U5 pad 1: Net-(U3-Pad1) -> Net-(C16-Pad1)
- U5 pad 12: Net-(J4-Pad3) -> Net-(J1-Pad3)
- U5 pad 14: Net-(U3-Pad14) -> Net-(C17-Pad1)
- Y1 pad 1: Net-(U3-Pad14) -> Net-(C17-Pad1)
- Y1 pad 2: Net-(U3-Pad1) -> Net-(C16-Pad1)
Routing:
- net GND: track 489.5 -> 176.9 mm, vias 115 -> 124
- net V5P0: track 133.3 -> 1.95 mm, vias 3 -> 4
- net VAC: track 128.5 -> 12.8 mm, vias 2 -> 1
- net V3P3: track 220.9 -> 126.3 mm, vias 47 -> 56
- net VREF_AH: track 93.0 -> 0.00 mm, vias 2 -> 0
- net V12P0: track 92.7 -> 6.11 mm, vias 2 -> 5
- net /arduino_header/A7: track 42.5 -> 0.00 mm, vias 1 -> 0
- net /arduino_header/A6: track 41.5 -> 0.00 mm, vias 1 -> 0
- net VCC5V: track 49.3 -> 12.6 mm, vias 6 -> 5
- net V1P8: track 34.3 -> 0.70 mm, vias 7 -> 1
- net Net-(R38-Pad1): track 25.8 -> 0.00 mm
- net /power_2/RESET_ASIC: track 24.4 -> 0.00 mm, vias 3 -> 0
- net Net-(J8-Pad1): track 20.0 -> 0.00 mm, vias 0 -> 4
- net Net-(FB3-Pad1): track 17.4 -> 0.00 mm
- net Net-(C67-Pad1): track 19.2 -> 2.74 mm, vias 7 -> 5
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- added copper zone on B.Cu, net GND
- added copper zone on In2.Cu, net GND
- added copper zone on B.Cu, net Net-(C67-Pad1)
- added copper zone on B.Cu, net Net-(C71-Pad1)
- added copper zone on F.Cu, net Net-(C71-Pad1)
- added copper zone on In2.Cu, net Net-(C71-Pad1)
- added copper zone on B.Cu, net Net-(C91-Pad1)
- added copper zone on F.Cu, net Net-(C91-Pad1)
- added copper zone on In2.Cu, net Net-(C91-Pad1)
- added copper zone on B.Cu, net Net-(F1-Pad2)
- added copper zone on In2.Cu, net Net-(F1-Pad2)
- added copper zone on B.Cu, net Net-(J19-Pad3)
- added copper zone on F.Cu, net Net-(J19-Pad3)
- added copper zone on In2.Cu, net Net-(J19-Pad3)
- added copper zone on B.Cu, net Net-(J8-Pad1)
- added copper zone on In2.Cu, net Net-(J8-Pad1)
- added copper zone on B.Cu, net V12P0
- added copper zone on In2.Cu, net V12P0
- added copper zone on B.Cu, net VCC5V
- removed copper zone on In1.Cu, net GND
- removed copper zone on F.Cu, net Net-(C56-Pad1)
- removed copper zone on F.Cu, net Net-(C62-Pad1)
- removed copper zone on F.Cu, net Net-(C90-Pad2)
- removed copper zone on F.Cu, net Net-(J6-Pad1)
- removed copper zone on In2.Cu, net Net-(J6-Pad1)
- removed copper zone on F.Cu, net V1P8
- removed copper zone on In2.Cu, net V1P8
- removed copper zone on F.Cu, net V3P3
- removed copper zone on F.Cu, net V5P0
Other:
- board outline removed
- net class Default: trace_width 0.25 -> 0.2032; via_dia 0.8 -> 0.4064; via_drill 0.4 -> 0.2032
- net class sdram added: clearance 0.2032, trace_width 0.2032, via_dia 0.4064, via_drill 0.2032
- rule trace_min: 0.2032 -> 0
- rule via_min_drill: 0.3 -> 0.2032
- rule via_min_size: 0.3 -> 0.254
- board text added: "+Ve"
- board text added: "+ve"
- board text added: "-Ve"
- board text added: "-ve"
- board text added: "1"
- board text added: "10"
- board text added: "11"
- board text added: "12"
- board text added: "15"
- board text added: "16"
- board text added: "17"
- board text added: "2"
- board text added: "20"
- board text added: "3"
- board text added: "32"
- board text added: "33"
- board text added: "3v3"
- board text added: "4"
- board text added: "43"
- board text added: "44"
- board text added: "48"
- board text added: "49"
- board text added: "5"
- board text added: "6"
- board text added: "64"
- board text added: "8"
- board text added: "86"
- board text added: "9"
- board text added: "A"
- board text added: "A0"
- board text added: "A1"
- board text added: "A2"
- board text added: "A3"
- board text added: "A4"
- board text added: "A5"
- board text added: "A6"
- board text added: "A7"
- board text added: "Boot_Mode0"
- board text added: "Boot_Mode1"
- board text added: "CLK"
- board text added: "GND"
- board text added: "Gnd"
- board text added: "I2C1_SCL"
- board text added: "IO0"
- board text added: "IO1"
- board text added: "IO2"
- board text added: "IO3"
- board text added: "IO_0"
- board text added: "IO_13"
- board text added: "IO_14"
- board text added: "IO_7"
- board text added: "IO_8"
- board text added: "K"
- board text added: "MOSI"
- board text added: "NC"
- board text added: "NCS"
- board text added: "NCS_F"
- board text added: "NCS_H"
- board text added: "QSPI0"
- board text added: "RST"
- board text added: "SCL"
- board text added: "SDA"
- board text added: "SPI1_MISO"
- board text added: "TCK"
- board text added: "TDI"
- board text added: "TDO"
- board text added: "TMS"
- board text added: "TRST"
- board text added: "Test_Mode"
- board text added: "V12P0"
- board text added: "V3P3"
- board text added: "V5P0"
- board text added: "V5P0(I/P)"
- board text added: "V5P0(O/P)"
- board text added: "VAC"
- board text added: "VBUS"
- board text added: "VBUS_USB1"
- board text added: "VBUS_USB2"
- board text added: "VREF"
- board text added: "nCS"
